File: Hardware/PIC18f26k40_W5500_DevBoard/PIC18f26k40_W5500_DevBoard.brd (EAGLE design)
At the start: 59 x 65 mm, 48 parts, among them J2 MAGJACK, J6 USB-B, U1 W5500, U2 PIC18F2523-I/SO

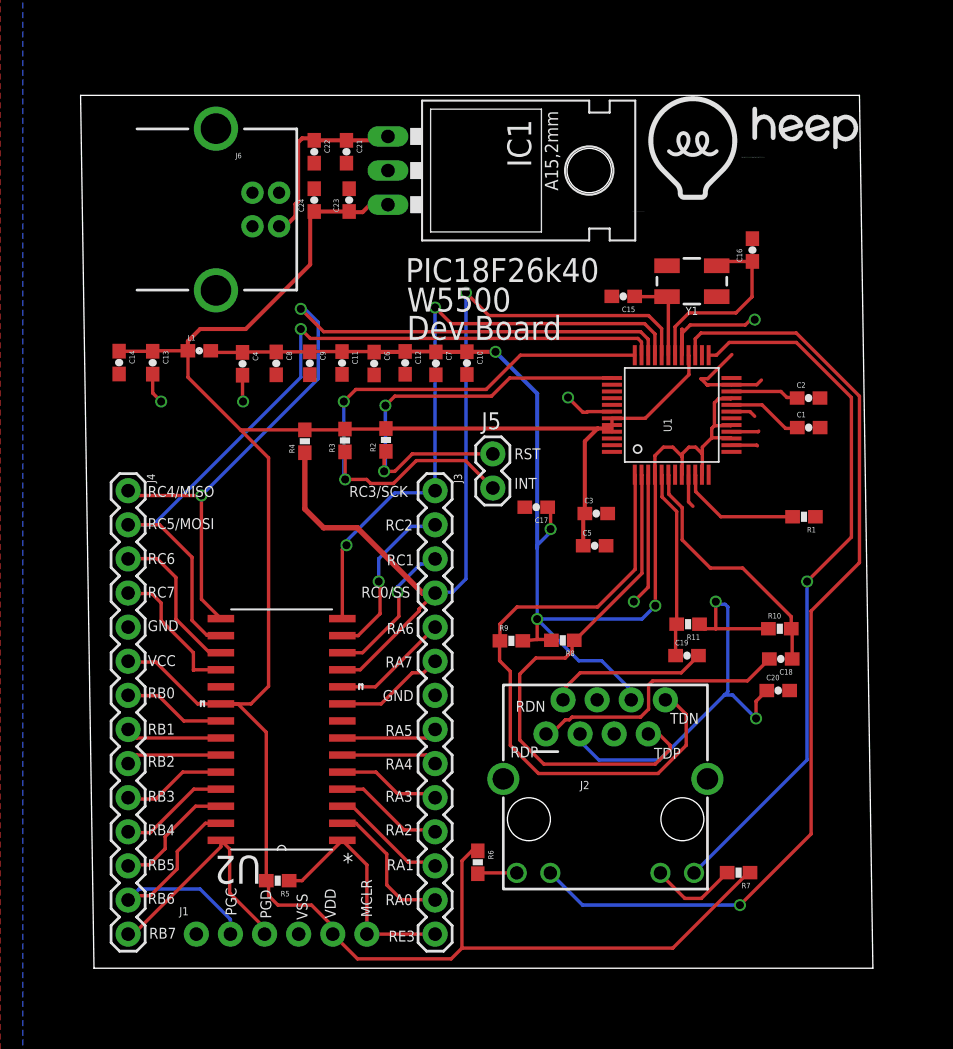
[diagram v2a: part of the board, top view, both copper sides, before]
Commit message: #251 Straightened out sides of circuit board
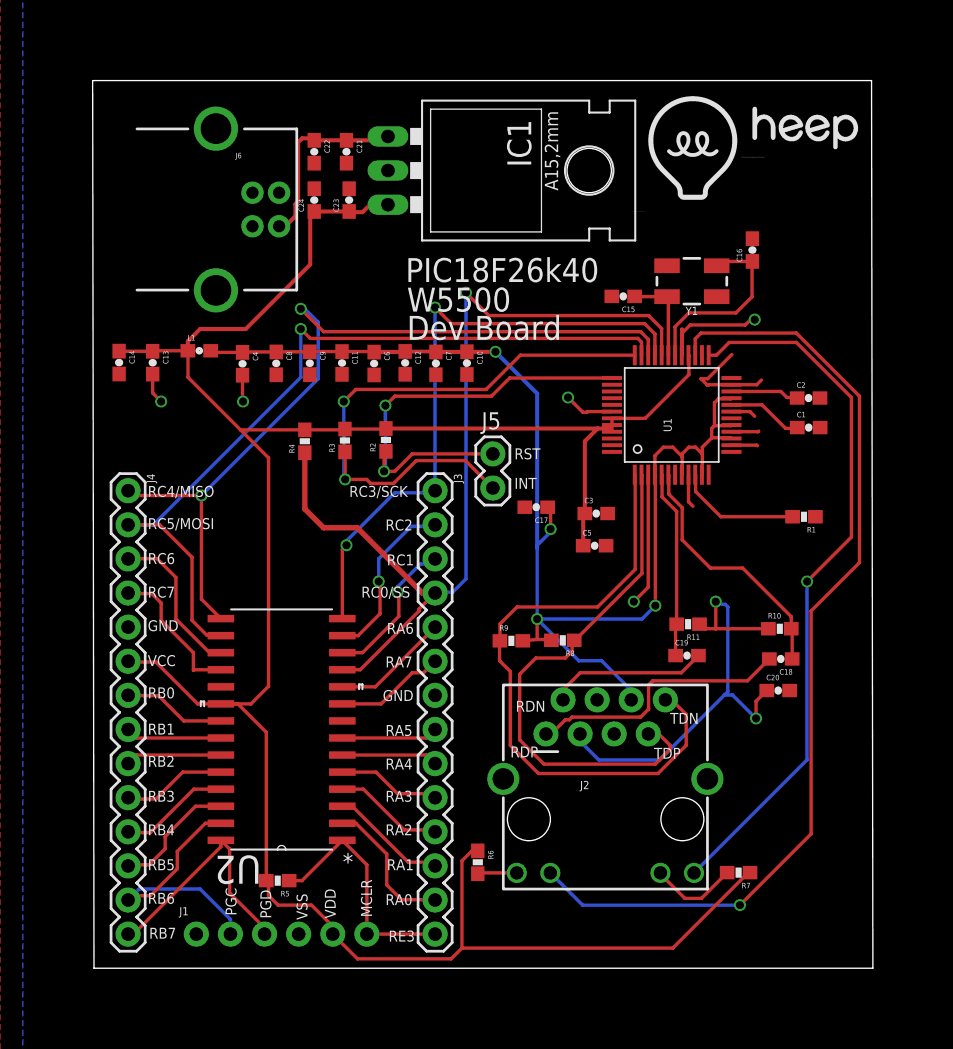
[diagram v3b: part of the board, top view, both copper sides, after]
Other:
- board size 59 x 65 mm -> 58.1 x 66.1 mm
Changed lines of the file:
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@@
 <plain>
 <wire x1="0" y1="0" x2="58" y2="0" width="0" layer="20"/>
-<wire x1="58" y1="0" x2="57" y2="65" width="0" layer="20"/>
-<wire x1="57" y1="65" x2="-1" y2="65" width="0" layer="20"/>
-<wire x1="-1" y1="65" x2="0" y2="0" width="0" layer="20"/>
+<wire x1="58" y1="0" x2="57.9" y2="66.1" width="0" layer="20"/>
+<wire x1="57.9" y1="66.1" x2="-0.1" y2="66.1" width="0" layer="20"/>
+<wire x1="-0.1" y1="66.1" x2="0" y2="0" width="0" layer="20"/>
 <text x="23.2" y="51.1" size="1.778" layer="21">PIC18F26k40</text>
 <text x="23.3" y="48.9" size="1.778" layer="21">W5500</text>

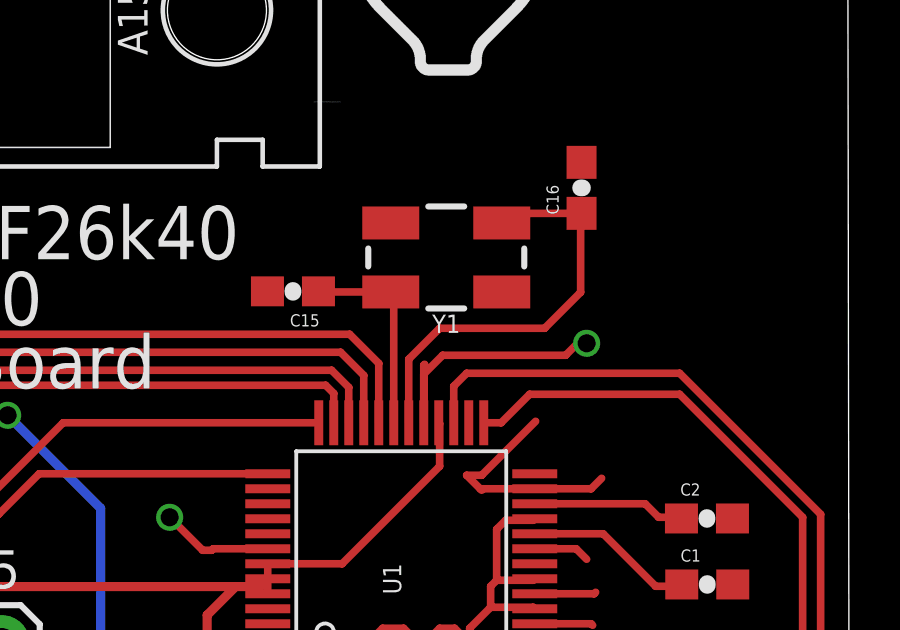
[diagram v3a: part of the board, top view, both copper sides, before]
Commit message: #251 Fixed crystal in schematic
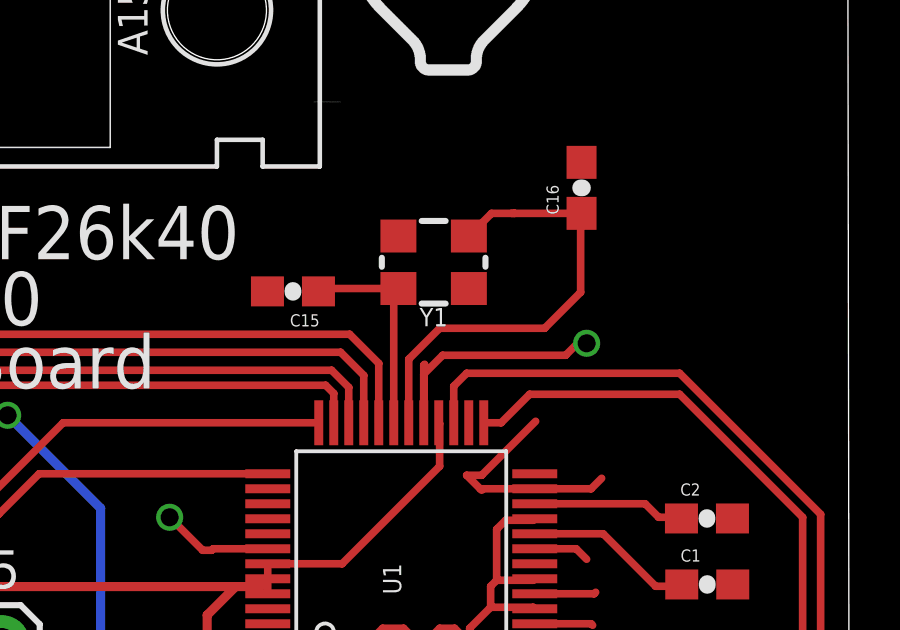
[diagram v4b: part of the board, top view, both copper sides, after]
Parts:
- C15, C16: value 15pF -> 8pF
- Y1: device SparkFun-Clocks:CRYSTAL-SMD-5X3.2-4PAD -> SparkFun-Clocks:CRYSTAL-SMD-3.2X2.5MM
- moved Y1 0.45 mm to (44.1, 51.0)
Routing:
- net N$6: track 14.2 -> 15.6 mm
- net N$5: track 6.82 -> 7.42 mm
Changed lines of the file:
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@@
 <element name="C13" library="SparkFun-Passives" package="0603-CAP" value="10uF" x="4.37" y="45.09" rot="R270"/>
 <element name="C14" library="SparkFun-Passives" package="0603-CAP" value="100nF" x="1.87" y="45.1" rot="R270"/>
-<element name="C15" library="SparkFun-Passives" package="0603-CAP" value="15pF" x="39.41" y="50.03" rot="R180"/>
-<element name="C16" library="SparkFun-Passives" package="0603-CAP" value="15pF" x="49.03" y="53.48" rot="R90"/>
+<element name="C15" library="SparkFun-Passives" package="0603-CAP" value="8pF" x="39.41" y="50.03" rot="R180"/>
+<element name="C16" library="SparkFun-Passives" package="0603-CAP" value="8pF" x="49.03" y="53.48" rot="R90"/>
 <element name="C17" library="SparkFun-Passives" package="0603-CAP" value="100nF" x="32.93" y="34.33" rot="R180"/>
 <element name="C18" library="SparkFun-Passives" package="0603-CAP" value="6.8nF" x="51.14" y="23.03" rot="R180"/>
@@
 <attribute name="VALUE" x="13.2884" y="32.1072" size="2.0828" layer="27" ratio="10" rot="SR270"/>
 </element>
-<element name="Y1" library="SparkFun-Clocks" package="CRYSTAL-SMD-5X3.2-4PAD" value="" x="44.52" y="51.16" rot="R180"/>
 <element name="U$5" library="Heep" package="HEEPLOGOSMALL" value="" x="40.1" y="56.4"/>
 <element name="U$6" library="Heep" package="HEEPLETTERS" value="" x="48.2" y="60.5"/>
@@
 <element name="C23" library="SparkFun-Passives" package="0603-CAP" value="10uF" x="19" y="57.2" rot="R90"/>
 <element name="C24" library="SparkFun-Passives" package="0603-CAP" value="0.1uF" x="16.4" y="57.2" rot="R90"/>
+<element name="Y1" library="SparkFun-Clocks" package="CRYSTAL-SMD-3.2X2.5MM" value="" x="44.1" y="51" rot="R180"/>
 </elements>
 <signals>
@@
 <signal name="N$5">
 <contactref element="U1" pad="31"/>
+<contactref element="C15" pad="1"/>
+<wire x1="40.26" y1="50.03" x2="40.28" y2="50.01" width="0.254" layer="1"/>
 <contactref element="Y1" pad="3"/>
-<contactref element="C15" pad="1"/>
-<wire x1="42.77" y1="45.65" x2="42.77" y2="49.91" width="0.254" layer="1"/>
-<wire x1="42.77" y1="49.91" x2="42.67" y2="50.01" width="0.254" layer="1"/>
-<wire x1="42.67" y1="50.01" x2="40.28" y2="50.01" width="0.254" layer="1"/>
-<wire x1="40.28" y1="50.01" x2="40.26" y2="50.03" width="0.254" layer="1"/>
+<wire x1="40.26" y1="50.125" x2="42.925" y2="50.125" width="0.254" layer="1"/>
+<wire x1="40.26" y1="50.125" x2="40.26" y2="50.03" width="0.254" layer="1"/>
+<wire x1="42.925" y1="50.125" x2="42.77" y2="50.125" width="0.254" layer="1"/>
+<wire x1="42.77" y1="50.125" x2="42.77" y2="45.65" width="0.254" layer="1"/>
 </signal>
 <signal name="N$6">
 <contactref element="U1" pad="30"/>
-<contactref element="Y1" pad="1"/>
 <contactref element="C16" pad="1"/>
 <wire x1="43.27" y1="45.65" x2="43.27" y2="47.77" width="0.254" layer="1"/>
@@
 <wire x1="49" y1="50" x2="49" y2="52.6" width="0.254" layer="1"/>
 <wire x1="49" y1="52.6" x2="49.03" y2="52.63" width="0.254" layer="1"/>
-<wire x1="49.03" y1="52.63" x2="46.69" y2="52.63" width="0.254" layer="1"/>
-<wire x1="46.69" y1="52.63" x2="46.37" y2="52.31" width="0.254" layer="1"/>
+<wire x1="49.03" y1="52.63" x2="46.8" y2="52.63" width="0.254" layer="1"/>
+<contactref element="Y1" pad="1"/>
+<wire x1="46.8" y1="52.63" x2="46.69" y2="52.63" width="0.254" layer="1"/>
+<wire x1="46.8" y1="52.63" x2="46.03" y2="52.63" width="0.254" layer="1"/>
+<wire x1="46.03" y1="52.63" x2="45.275" y2="51.875" width="0.254" layer="1"/>
 </signal>
 <signal name="ACTLED">

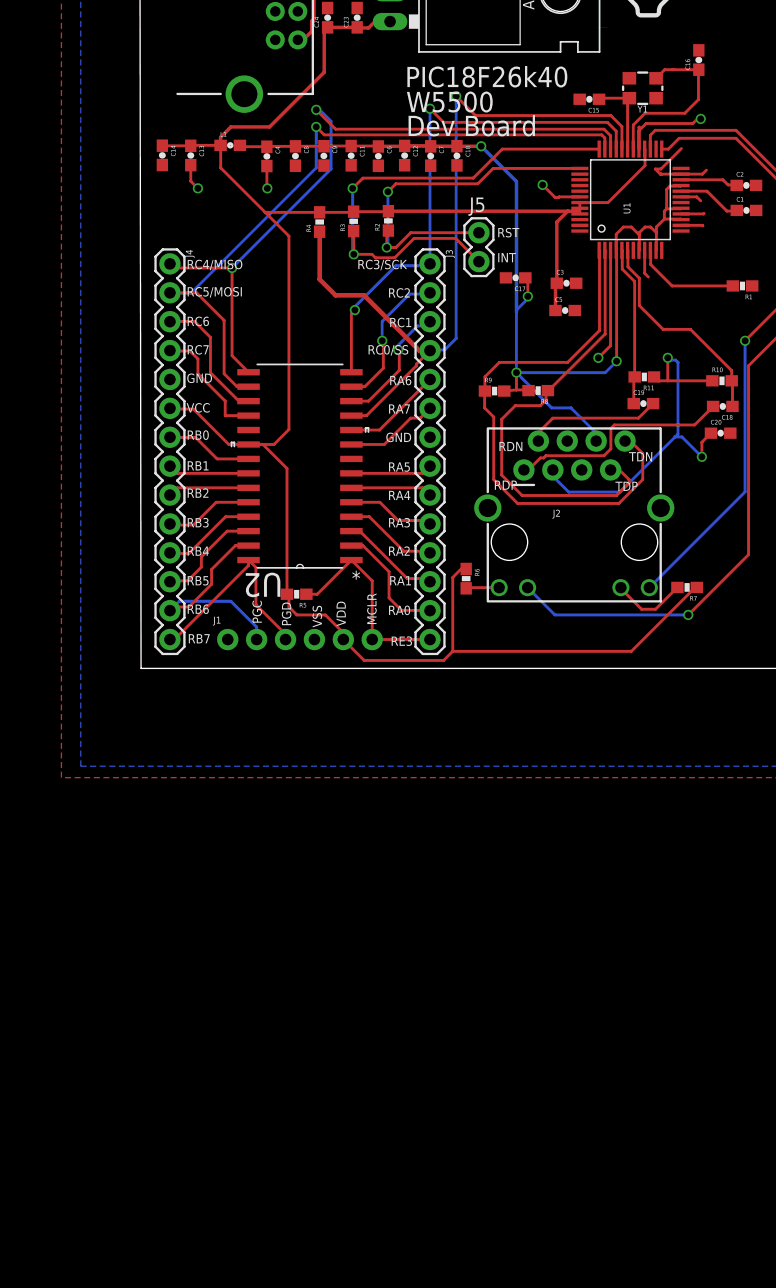
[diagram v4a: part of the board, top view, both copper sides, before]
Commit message: #302 Added pull up and pull down resistors to Wiznet direction connections
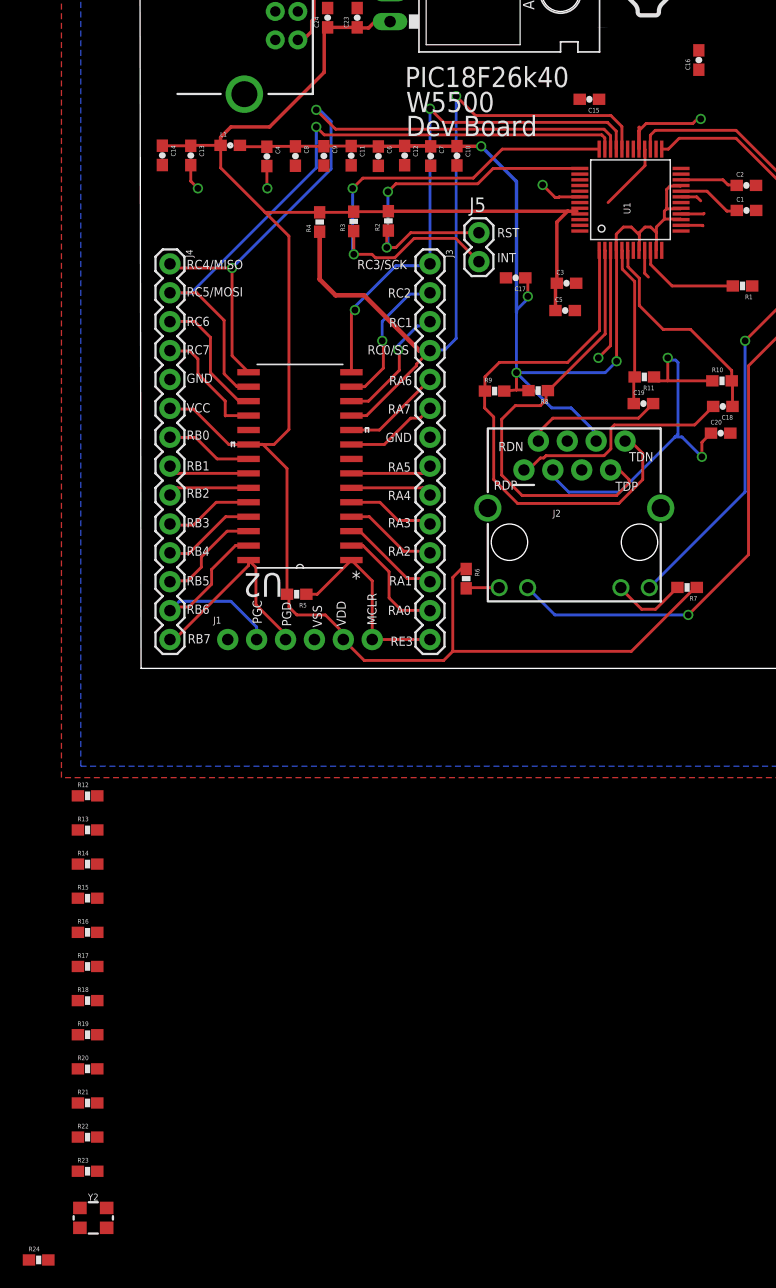
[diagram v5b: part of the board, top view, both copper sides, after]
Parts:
- removed Y1: (no value), SparkFun-Clocks:CRYSTAL-SMD-3.2X2.5MM
- added R12, R13, R14, R15, R16, R17, R18, R19, R20, R21, R22, R23: 10k, SparkFun-Passives:0603-RES
- added R24: 1Meg, SparkFun-Passives:0603-RES
- added Y2: CRYSTAL-GROUNDEDSMD-3.2X2.5, SparkFun-Clocks:CRYSTAL-SMD-3.2X2.5MM
- C2: value 10uF -> 10nF
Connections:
- removed net N$5: C15.1, U1.31, Y1.3
- new net N$12: R14.1, U1.38
- new net N$13: R15.1, U1.39
- new net N$14: R16.1, U1.40
- new net N$15: R13.1, U1.42
- new net N$16: R23.1, U1.23
- new net N$17: C16.1, R24.1, U1.30, Y2.1
- new net N$3: R12.1, U1.41
- new net PMODE0: R17.2, R18.1, U1.45
- new net PMODE1: R19.2, R20.1, U1.44
- new net PMODE2: R21.1, R22.2, U1.43
- net GND: now also R12.2, R13.2, R14.2, R15.2, R16.2, R18.2, R20.2, R21.2, R23.2, Y2.2, Y2.4; no longer U1.23, U1.38, U1.39, U1.40, U1.41, U1.42
- net N$6: now also C15.1, R24.2, U1.31, Y2.3; no longer C16.1, U1.30, Y1.1
- net VCC: now also R17.1, R19.1, R22.1; no longer U1.43, U1.44, U1.45
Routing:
- net N$6: track 15.6 -> 0.00 mm
- net GND: track 44.1 -> 32.4 mm, vias 5 -> 4
- net N$5: track 7.42 -> 0.00 mm
- net VCC: track 178.7 -> 174.9 mm
- net N$15: track 0.00 -> 3.75 mm, vias 0 -> 1

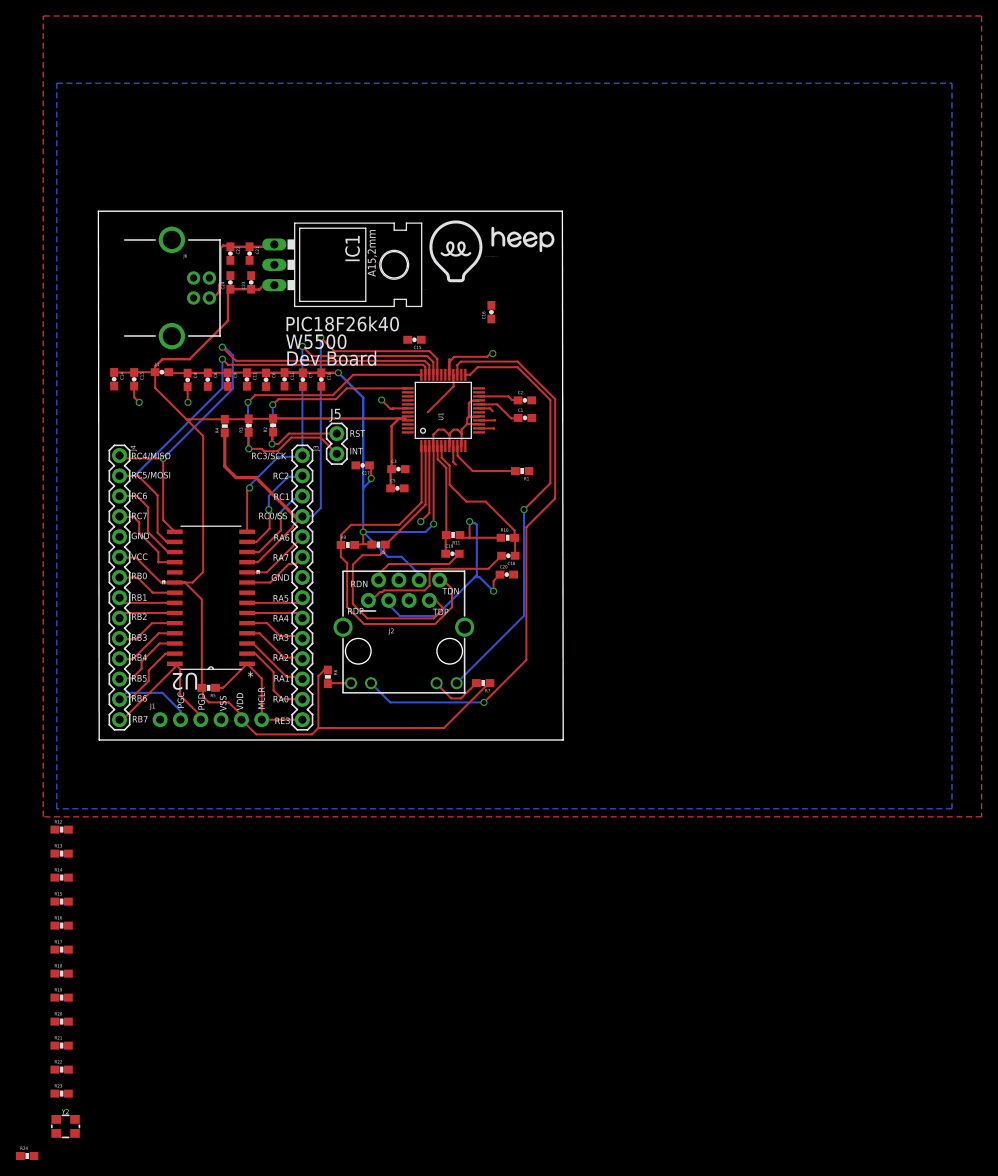
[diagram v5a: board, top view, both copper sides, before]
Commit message: #302 Most of new board routed
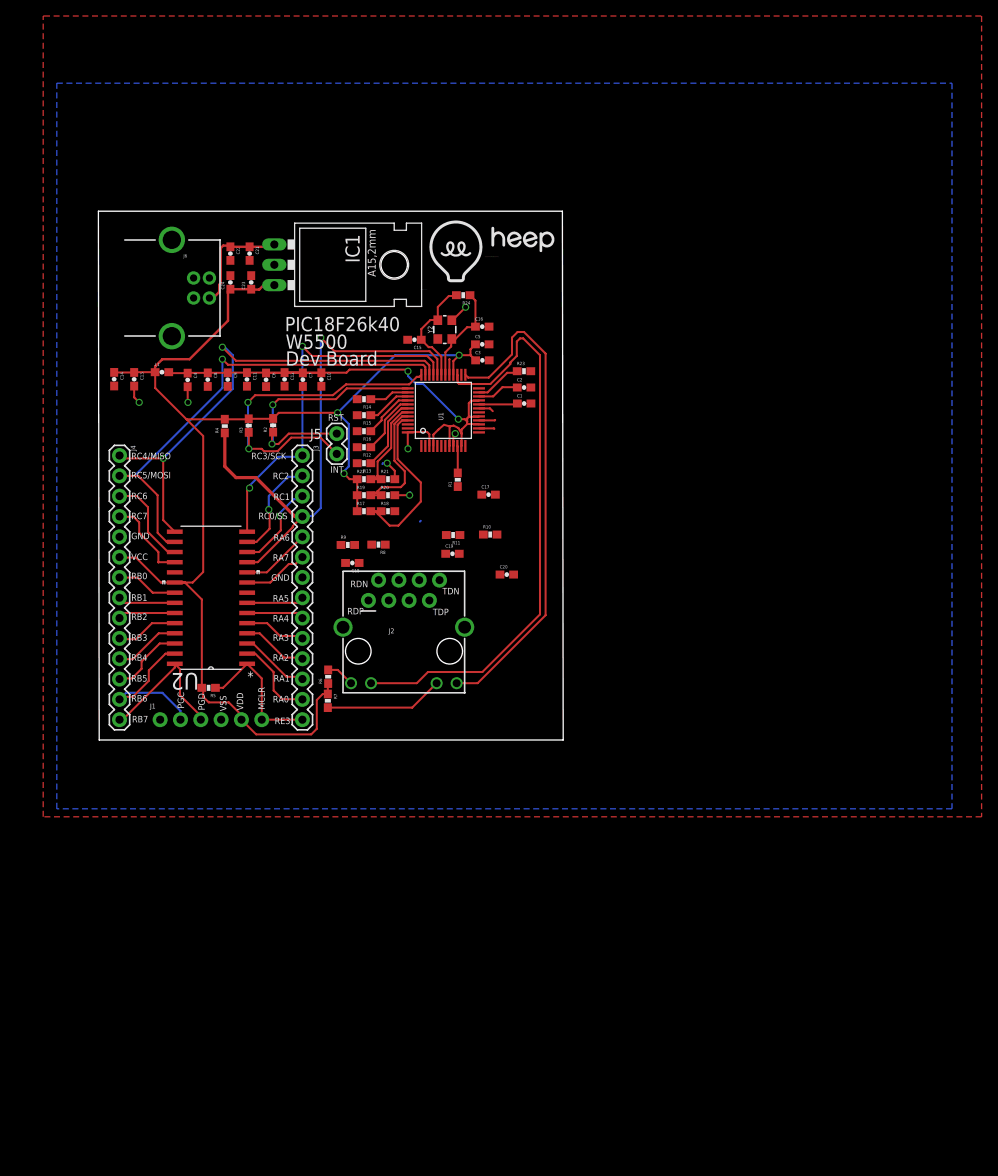
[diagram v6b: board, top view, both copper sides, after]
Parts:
- moved R24 120.6 mm to (45.5, 55.6), turned to 180 degrees
- moved Y2 110.3 mm to (43.2, 51.3), turned to 90 degrees
- moved R23 107.2 mm to (53.1, 46.1)
- moved R22 82.9 mm to (33.1, 32.6)
- moved R21 81.7 mm to (36.1, 32.6)
- moved R20 77.4 mm to (36.1, 30.6)
- moved R19 73.3 mm to (33.1, 30.6)
- moved R16 72.4 mm to (33.1, 38.6), turned to 180 degrees
- moved R15 71.6 mm to (33.1, 40.6), turned to 180 degrees
- moved R18 70.7 mm to (36.1, 28.6)
- moved R14 70.7 mm to (33.1, 42.6), turned to 180 degrees
- moved R17 66.6 mm to (33.1, 28.6)
- moved R13 61.7 mm to (33.1, 34.6), turned to 180 degrees
- moved R12 60.9 mm to (33.1, 36.6), turned to 180 degrees
- moved C5 20.9 mm to (47.9, 49.5)
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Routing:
- net TDN: track 47.5 -> 0.00 mm
- net TDP: track 39.5 -> 0.00 mm
- net VCCA: track 102.9 -> 65.9 mm, vias 4 -> 2
- net N$11: track 34.4 -> 0.00 mm, vias 2 -> 0
- net PMODE0: track 0.00 -> 21.3 mm
- net N$8: track 20.0 -> 0.00 mm
- net RDP: track 18.9 -> 0.00 mm
- net PMODE1: track 0.00 -> 16.8 mm
- net N$6: track 0.00 -> 14.1 mm
- net RDN: track 14.0 -> 0.00 mm
- net PMODE2: track 0.00 -> 12.9 mm
- net N$17: track 0.00 -> 12.6 mm
- net N$10: track 11.9 -> 0.00 mm
- net VCC: track 174.9 -> 165.3 mm, vias 0 -> 3
- net LNKLED: track 53.0 -> 62.2 mm, vias 1 -> 0
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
